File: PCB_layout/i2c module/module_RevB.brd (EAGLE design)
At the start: 33.3 x 50 mm, 18 parts, among them IC1 ATTINY85-20SU, J1 M20-9980346, P1 PROTO_VIAS_01X01-1.2

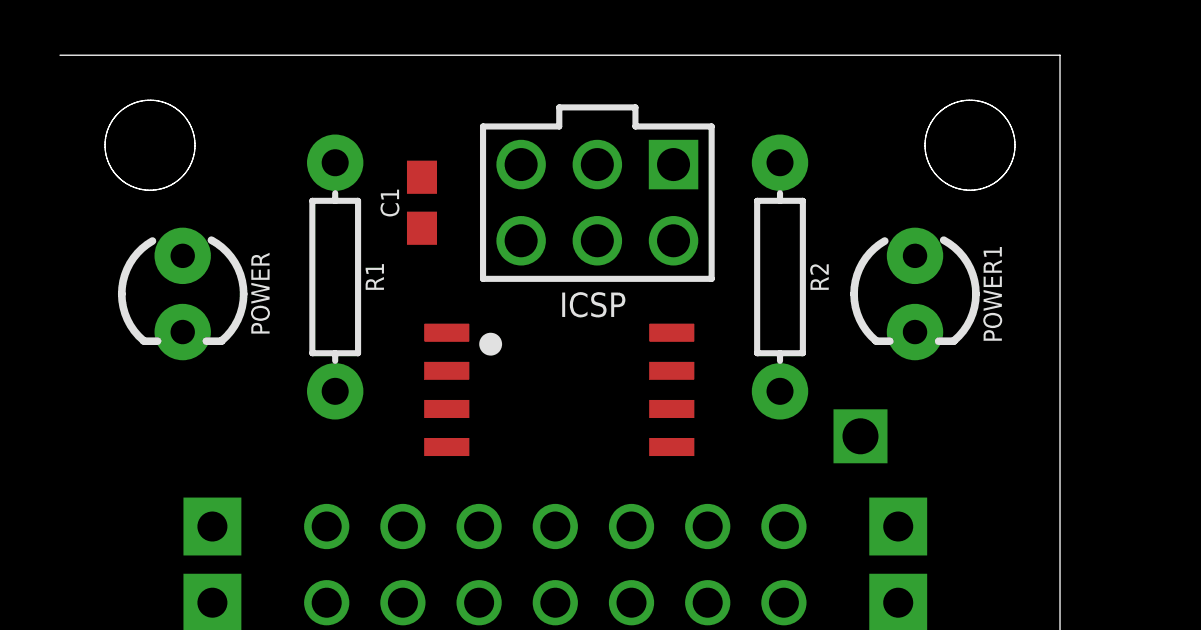
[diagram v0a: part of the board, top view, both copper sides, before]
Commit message: updated LED definition
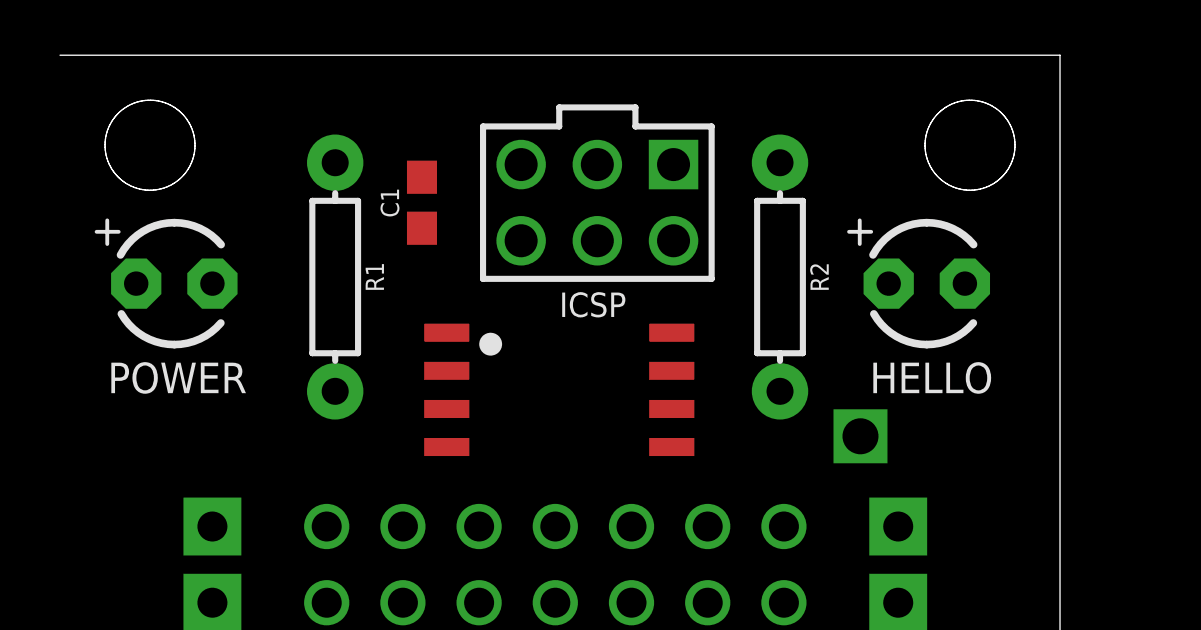
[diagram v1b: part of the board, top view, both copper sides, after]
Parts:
- removed POWER1: (no value), SparkFun-LED:LED_3MM
- added HELLO: LED3MM, BadgeParts:LED3MM
- POWER: value (none) -> LED3MM; device SparkFun-LED:LED_3MM -> BadgeParts:LED3MM
- moved POWER 0.44 mm to (3.81, 42.4), turned to 0 degrees
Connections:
- removed net N$11: POWER.A, R1.P$1
- new net N$3: HELLO.POS, R2.P$1
- net GND: now also HELLO.NEG, POWER.NEG; no longer POWER.K, POWER1.K
- net N$1: now also POWER.POS, R1.P$1; no longer POWER1.A, R2.P$1
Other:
- board text added: "HELLO"
- board text added: "POWER"
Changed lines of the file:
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@@
 <layer number="115" name="ReferenceISLANDS" color="7" fill="1" visible="yes" active="yes"/>
 <layer number="116" name="Patch_BOT" color="9" fill="4" visible="yes" active="yes"/>
+<layer number="117" name="BACKMAAT1" color="7" fill="1" visible="yes" active="yes"/>
 <layer number="118" name="Rect_Pads" color="7" fill="1" visible="yes" active="yes"/>
+<layer number="119" name="KAP_TEKEN" color="7" fill="1" visible="yes" active="yes"/>
+<layer number="120" name="KAP_MAAT1" color="7" fill="1" visible="yes" active="yes"/>
 <layer number="121" name="_tsilk" color="7" fill="1" visible="yes" active="yes"/>
 <layer number="122" name="_bsilk" color="7" fill="1" visible="yes" active="yes"/>
@@
 <layer number="128" name="_bValues" color="7" fill="1" visible="yes" active="yes"/>
 <layer number="129" name="Mask" color="7" fill="1" visible="yes" active="yes"/>
+<layer number="130" name="SMDSTROOK" color="7" fill="1" visible="yes" active="yes"/>
 <layer number="131" name="tAdjust" color="7" fill="1" visible="yes" active="yes"/>
 <layer number="132" name="bAdjust" color="7" fill="1" visible="yes" active="yes"/>
+<layer number="133" name="bottom_silk" color="7" fill="1" visible="yes" active="yes"/>
+<layer number="134" name="silk_top" color="7" fill="1" visible="yes" active="yes"/>
+<layer number="135" name="silk_bottom" color="7" fill="1" visible="yes" active="yes"/>
+<layer number="136" name="silktop" color="7" fill="1" visible="yes" active="yes"/>
+<layer number="137" name="silkbottom" color="7" fill="1" visible="yes" active="yes"/>
 <layer number="144" name="Drill_legend" color="7" fill="1" visible="yes" active="yes"/>
+<layer number="145" name="DrillLegend_01-16" color="7" fill="1" visible="yes" active="yes"/>
+<layer number="146" name="DrillLegend_01-20" color="7" fill="1" visible="yes" active="yes"/>
 <layer number="150" name="Notes" color="7" fill="1" visible="yes" active="yes"/>
 <layer number="151" name="HeatSink" color="7" fill="1" visible="yes" active="yes"/>
@@
 <layer number="154" name="FabDoc2" color="7" fill="1" visible="yes" active="yes"/>
 <layer number="155" name="FabDoc3" color="7" fill="1" visible="yes" active="yes"/>
+<layer number="166" name="AntennaArea" color="7" fill="1" visible="yes" active="yes"/>
+<layer number="168" name="4mmHeightArea" color="7" fill="1" visible="yes" active="yes"/>
 <layer number="199" name="Contour" color="7" fill="1" visible="yes" active="yes"/>
 <layer number="200" name="200bmp" color="1" fill="10" visible="yes" active="yes"/>
@@
 <wire x1="19.05" y1="17.78" x2="19.05" y2="10.16" width="0.1524" layer="21"/>
 <wire x1="21.59" y1="17.78" x2="21.59" y2="10.16" width="0.1524" layer="21"/>
+<text x="1.5875" y="38.735" size="1.016" layer="21" font="vector" ratio="15">POWER</text>
+<text x="26.9875" y="38.735" size="1.016" layer="21" font="vector" ratio="15">HELLO</text>
 </plain>
 <attributes>
@@
 <attribute name="PROD_ID" value=" " x="9.173" y="42.606" size="1.778" layer="27" font="vector" rot="R270" display="off"/>
 </element>
-<element name="POWER" library="SparkFun-LED" library_urn="urn:adsk.eagle:library:529" package="LED_3MM" package3d_urn="urn:adsk.eagle:package:39361/1" value="" x="4.09" y="42.042" rot="R270">
-<attribute name="PROD_ID" value="DIO-08794" x="4.09" y="42.042" size="1.778" layer="27" font="vector" rot="R270" display="off"/>
-</element>
 <element name="U$1" library="BadgeParts" package="HEMA-I2C" value="HEMA-I2C" x="8.89" y="0"/>
 <element name="R2" library="SparkFun-Resistors" library_urn="urn:adsk.eagle:library:532" package="AXIAL-0.3" package3d_urn="urn:adsk.eagle:package:39658/1" value="220" x="24" y="42.606" rot="R270">
 <attribute name="PROD_ID" value=" " x="24" y="42.606" size="1.778" layer="27" rot="R270" display="off"/>
-</element>
-<element name="POWER1" library="SparkFun-LED" library_urn="urn:adsk.eagle:library:529" package="LED_3MM" package3d_urn="urn:adsk.eagle:package:39361/1" value="" x="28.5" y="42.042" rot="R270">
-<attribute name="PROD_ID" value="DIO-08794" x="28.5" y="42.042" size="1.778" layer="27" rot="R270" display="off"/>
 </element>
 <element name="P1" library="dp_devices" package="PROTO_VIAS_01X01_1.2" value="PROTO_VIAS_01X01-1.2" x="26.6825" y="37.2975"/>
@@
 <attribute name="PROD_ID" value="CAP-08604" x="12.065" y="45.085" size="1.778" layer="27" rot="R90" display="off"/>
 </element>
+<element name="POWER" library="BadgeParts" package="LED3MM" value="LED3MM" x="3.81" y="42.38625"/>
+<element name="HELLO" library="BadgeParts" package="LED3MM" value="LED3MM" x="28.8925" y="42.38625"/>
 </elements>
 <signals>
@@
 <signal name="GND" class="2">
 <contactref element="U$1" pad="A"/>
-<contactref element="POWER" pad="K"/>
-<contactref element="POWER1" pad="K"/>
 <contactref element="GND" pad="P$10"/>
 <contactref element="GND" pad="P$1"/>
@@
 <contactref element="J1" pad="GND"/>
 <contactref element="C1" pad="1"/>
-<wire x1="15.3709375" y1="43.815" x2="28.5" y2="40.772" width="0" layer="19" extent="1-1"/>
+<contactref element="POWER" pad="NEG"/>
+<contactref element="HELLO" pad="NEG"/>
+<wire x1="12.065" y1="44.235" x2="15.3709375" y2="43.815" width="0" layer="19" extent="1-1"/>
 <wire x1="12.8909375" y1="36.938659375" x2="15.3709375" y2="43.815" width="0" layer="19" extent="1-1"/>
 <wire x1="5.08" y1="34.29" x2="12.8909375" y2="36.938659375" width="0" layer="19" extent="1-1"/>
@@
 <wire x1="5.08" y1="13.97" x2="5.08" y2="16.51" width="0" layer="19" extent="1-1"/>
 <wire x1="5.08" y1="11.43" x2="5.08" y2="13.97" width="0" layer="19" extent="1-1"/>
-<wire x1="4.09" y1="40.772" x2="5.08" y2="34.29" width="0" layer="19" extent="1-1"/>
 <wire x1="11.8744" y1="5.6068" x2="5.08" y2="11.43" width="0" layer="19" extent="1-1"/>
-<wire x1="12.065" y1="44.235" x2="11.8744" y2="5.6068" width="0" layer="19" extent="1-1"/>
-</signal>
-<signal name="N$11">
-<contactref element="R1" pad="P$1"/>
-<contactref element="POWER" pad="A"/>
-<wire x1="4.09" y1="43.312" x2="9.173" y2="46.416" width="0" layer="19" extent="1-1"/>
+<wire x1="5.08" y1="42.38625" x2="11.8744" y2="5.6068" width="0" layer="19" extent="1-1"/>
+<wire x1="30.1625" y1="42.38625" x2="5.08" y2="42.38625" width="0" layer="19" extent="1-1"/>
 </signal>
 <signal name="PB2">
@@
 <wire x1="14.8744" y1="5.6068" x2="15.24" y2="11.43" width="0" layer="19" extent="1-1"/>
 <wire x1="17.9109375" y1="46.355" x2="14.8744" y2="5.6068" width="0" layer="19" extent="1-1"/>
-</signal>
-<signal name="N$1">
-<contactref element="R2" pad="P$1"/>
-<contactref element="POWER1" pad="A"/>
-<wire x1="24" y1="46.416" x2="28.5" y2="43.312" width="0" layer="19" extent="1-1"/>
 </signal>
 <signal name="N$2">
@@
 <wire x1="20.4509375" y1="46.355" x2="12.7" y2="11.43" width="0" layer="19" extent="1-1"/>
 </signal>
+<signal name="N$1">
+<contactref element="R1" pad="P$1"/>
+<contactref element="POWER" pad="POS"/>
+<wire x1="2.54" y1="42.38625" x2="9.173" y2="46.416" width="0" layer="19" extent="1-1"/>
+</signal>
+<signal name="N$3">
+<contactref element="R2" pad="P$1"/>
+<contactref element="HELLO" pad="POS"/>
+<wire x1="27.6225" y1="42.38625" x2="24" y2="46.416" width="0" layer="19" extent="1-1"/>
+</signal>
 </signals>

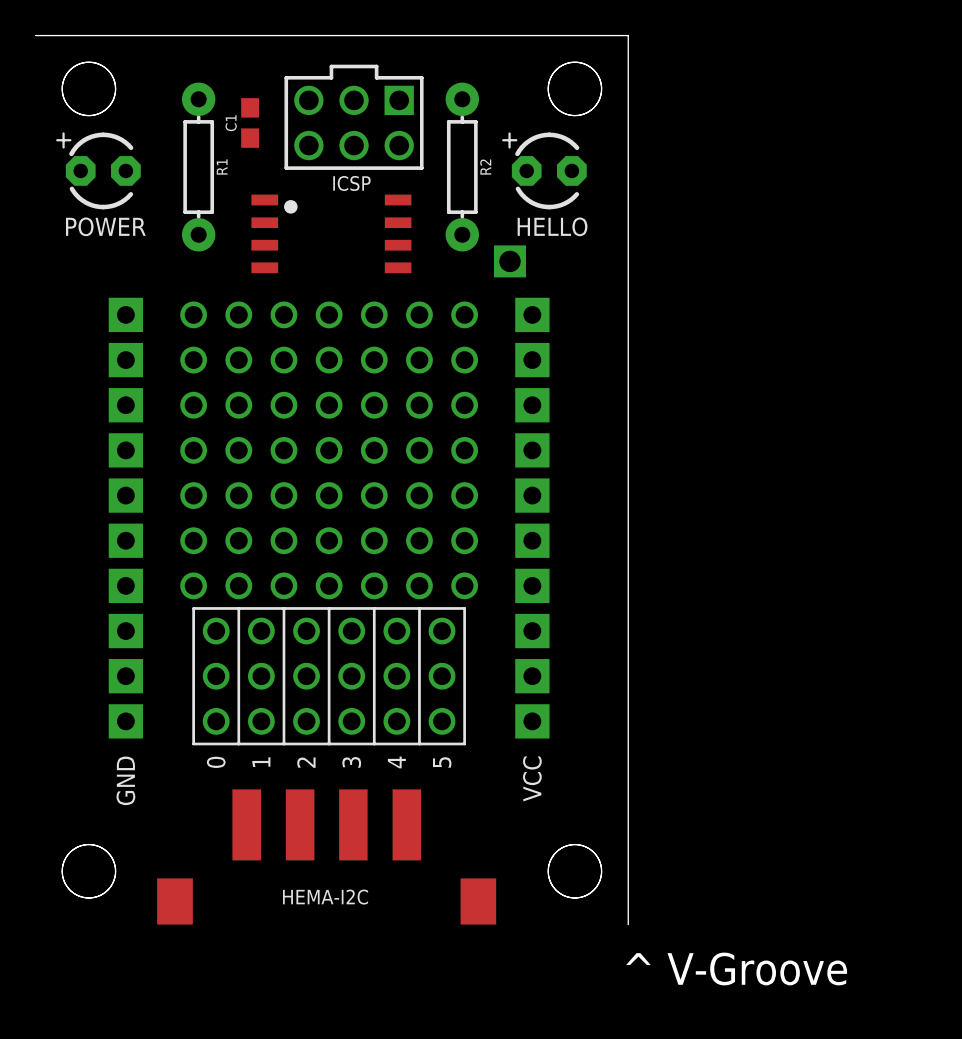
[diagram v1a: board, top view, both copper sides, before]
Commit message: swapped hema for 4p header; connect HW to D0, docu
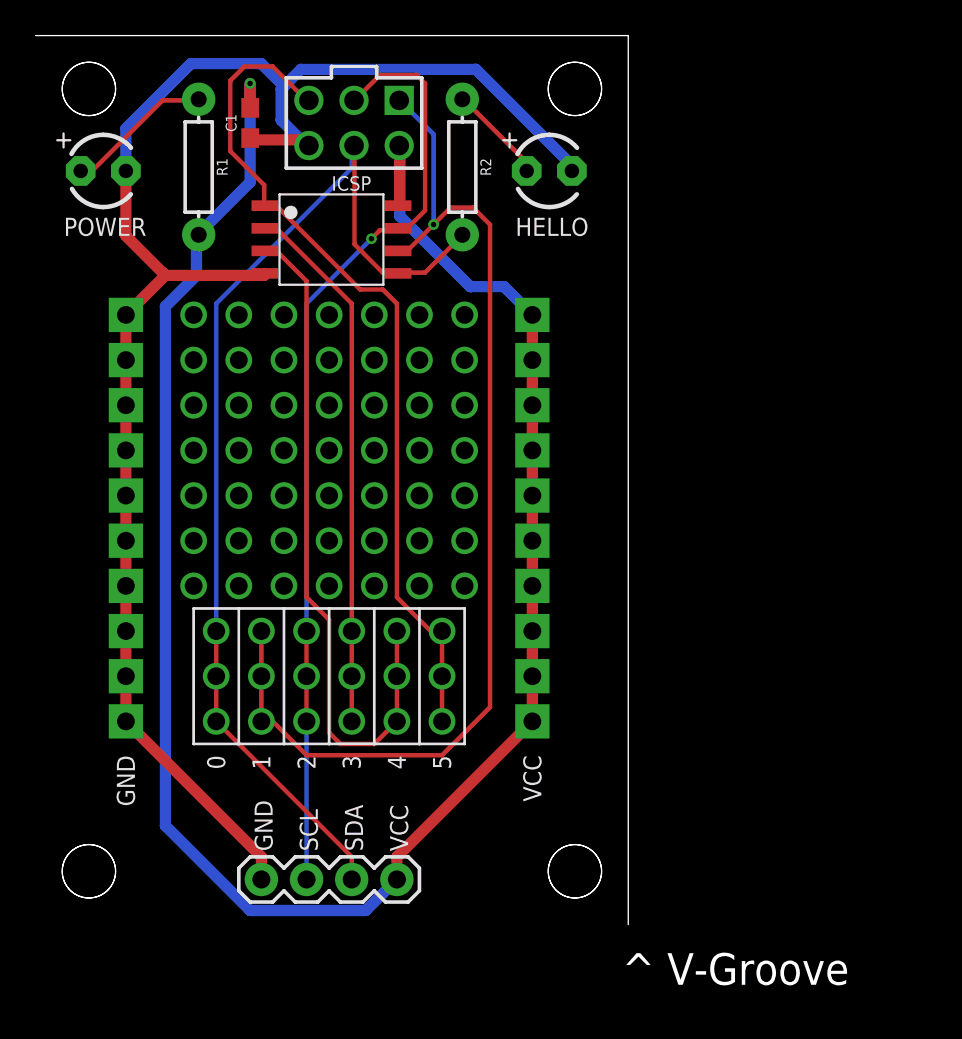
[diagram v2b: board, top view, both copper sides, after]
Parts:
- removed P1: PROTO_VIAS_01X01-1.2, dp_devices:PROTO_VIAS_01X01_1.2
- removed U$1: HEMA-I2C, BadgeParts:HEMA-I2C
- added J2: (no value), SparkFun-Connectors:1X04
- moved IC1 0.32 mm to (16.6, 38.5)
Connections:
- removed net N$2: P1.1, R2.P$2
- net GND: now also J2.1; no longer U$1.A
- net PB0: now also J2.3, R2.P$2; no longer U$1.C
- net PB2: now also J2.2; no longer U$1.B
- net VCC: now also J2.4; no longer U$1.D
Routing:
- net VCC: track 0.00 -> 112.9 mm, vias 0 -> 1
- net GND: track 0.00 -> 90.6 mm
- net PB1: track 0.00 -> 61.4 mm, vias 0 -> 1
- net PB0: track 0.00 -> 60.9 mm
- net PB2: track 0.00 -> 53.2 mm, vias 0 -> 1
- net PB5: track 0.00 -> 48.0 mm
- net PB4: track 0.00 -> 38.7 mm
- net PB3: track 0.00 -> 30.1 mm
- net N$1: track 0.00 -> 8.29 mm
- net N$3: track 0.00 -> 5.56 mm
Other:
- board text added: "GND"
- board text added: "SCL"
- board text added: "SDA"
- board text added: "VCC"
